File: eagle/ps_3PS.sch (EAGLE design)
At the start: 12 parts, among them J1 PIN2F061.100, J2 PIN2F061.100

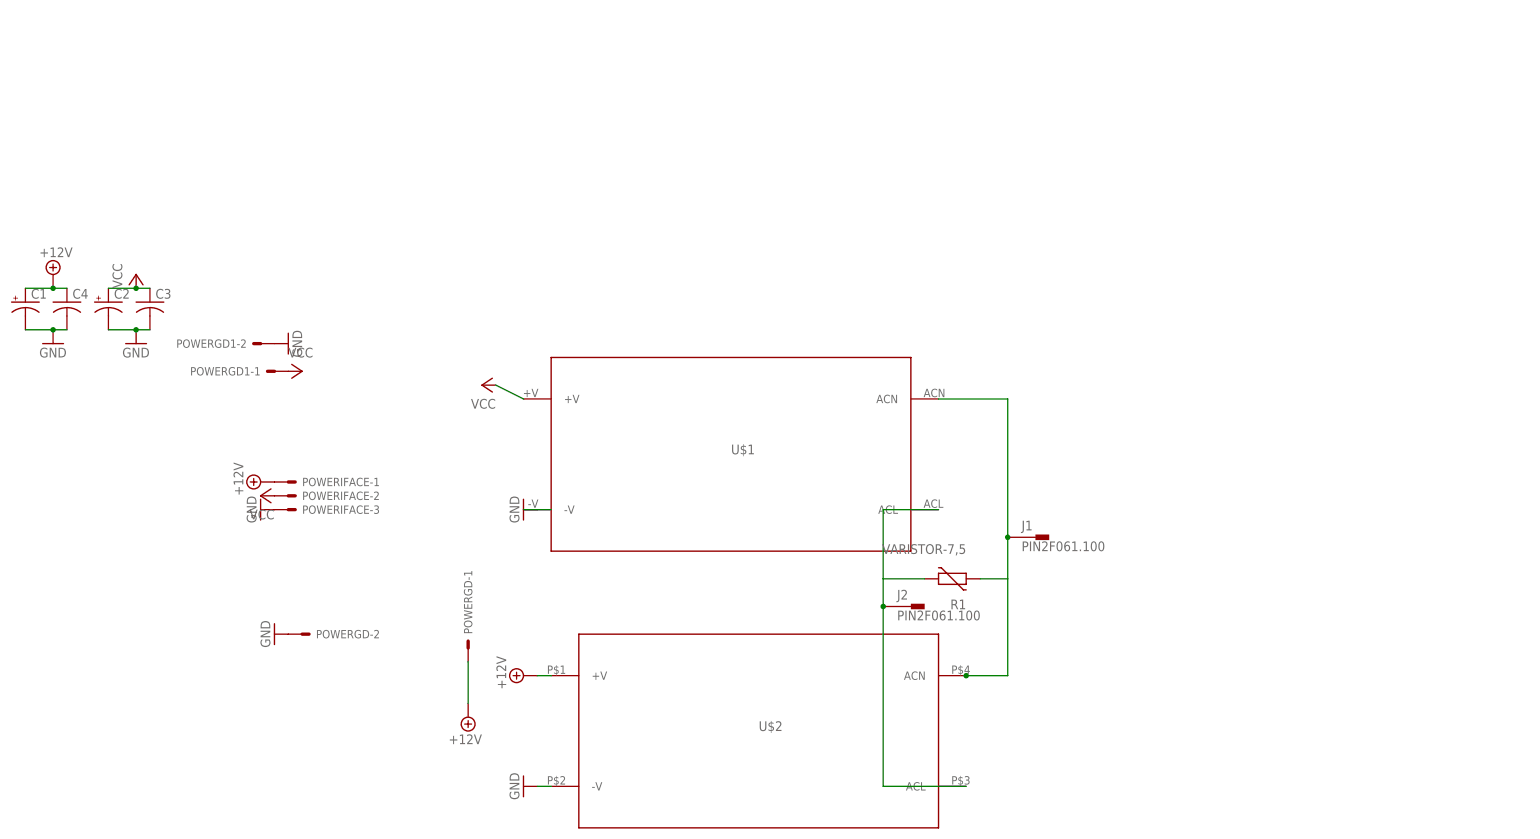
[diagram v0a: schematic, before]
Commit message: tweaks. still need bigger vias for zeners and hv resistors
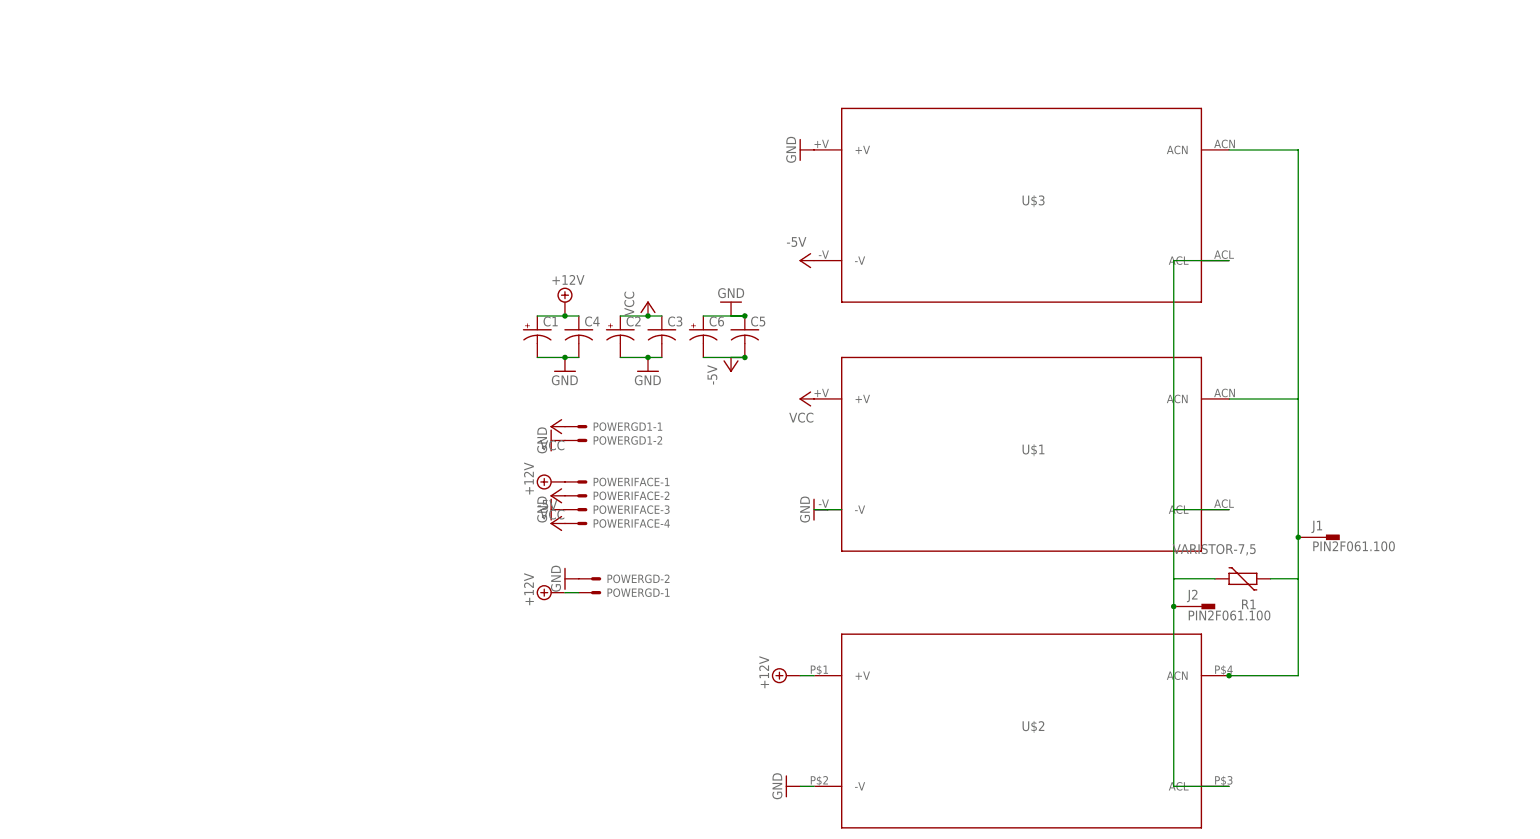
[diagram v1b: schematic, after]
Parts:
- added C5: (no value), rcl:C-US050-050X075
- added C6: (no value), rcl:CPOL-USE5-13
- added U$3: IRM-05-05, meanwell:IRM-05-05
- POWERIFACE: device con-molex:KK-156-3 -> con-molex:KK-156-4
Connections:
- new net -5V: C5.2, C6.-, POWERIFACE-4.S, U$3.-V
- net GND: now also C5.1, C6.+, U$3.+V
- net N$1: now also U$3.ACN
- net N$2: now also U$3.ACL
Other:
- moved on the sheet: C1, C2, C3, C4, J1, J2, POWERGD-1, POWERGD-2, POWERGD1-1, POWERGD1-2, POWERIFACE-1, POWERIFACE-2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

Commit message: optional 317 regulation of emcos
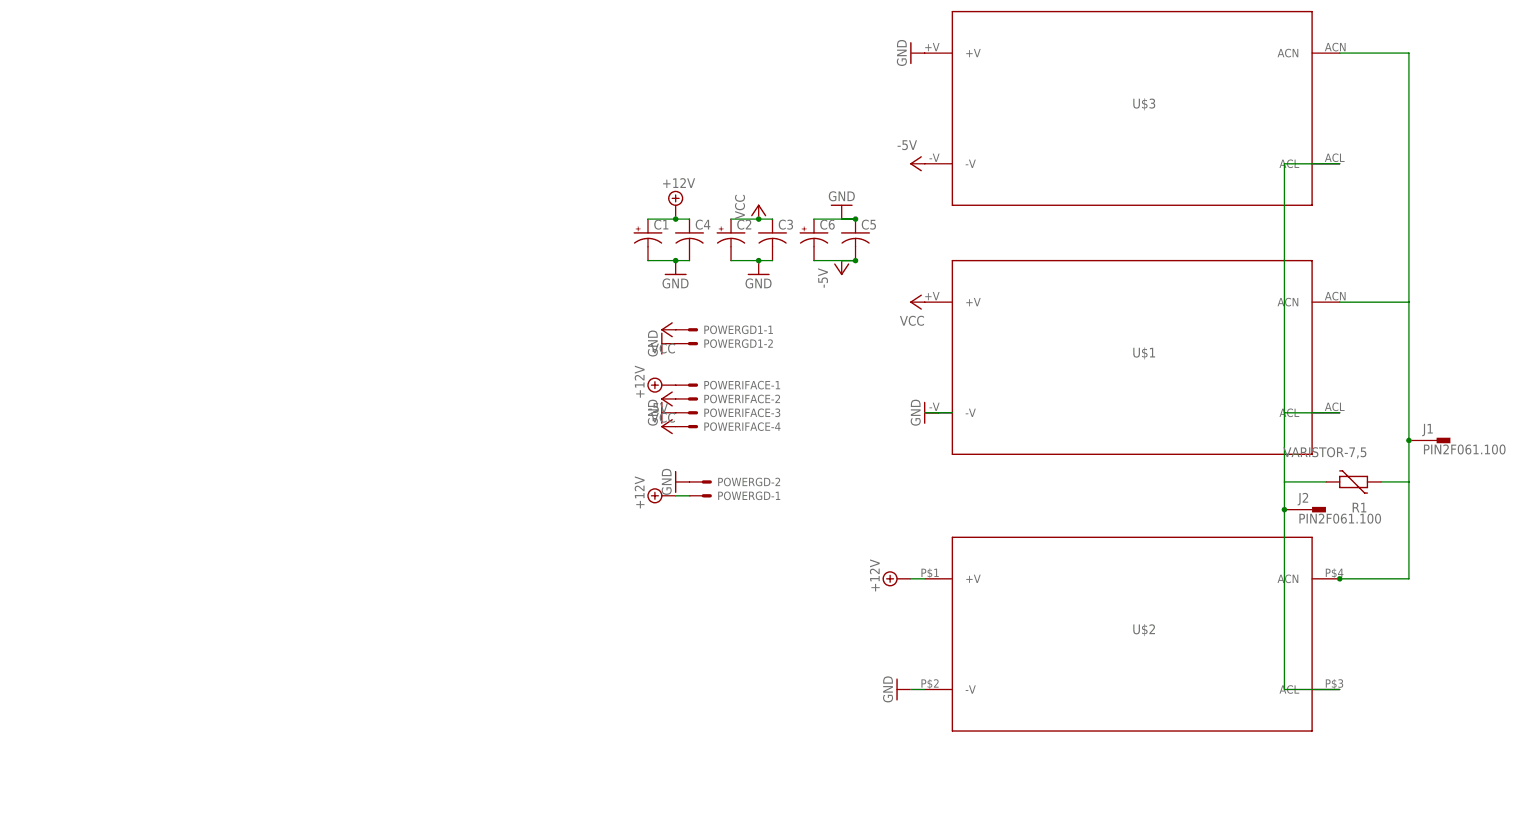
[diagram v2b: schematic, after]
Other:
- moved on the sheet: C1, C2, C3, C4, C5, C6, J1, J2, POWERGD-1, POWERGD-2, POWERGD1-1, POWERGD1-2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
